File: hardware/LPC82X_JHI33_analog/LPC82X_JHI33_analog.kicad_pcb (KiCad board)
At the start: 2 copper layers, 23.6 x 23.5 mm, 24 parts, among them J1 LPC82XJHI33_LEFT, J2 LPC82XJHI33_RIGHT, J3 JTAG_2X05, U1 LPC824M201JHI33, Y1 12MHz

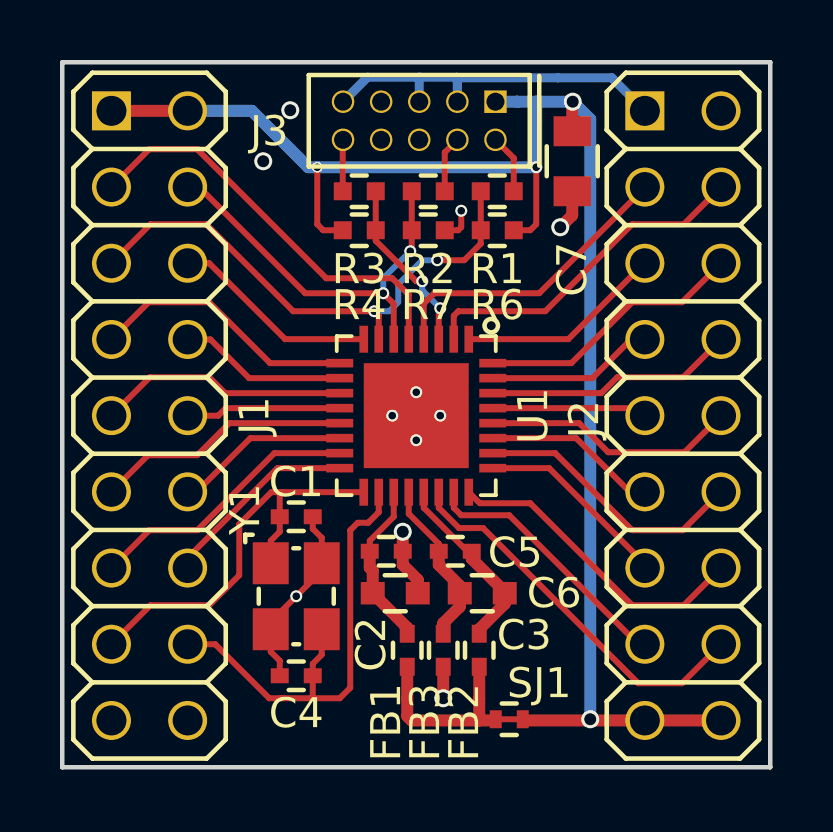
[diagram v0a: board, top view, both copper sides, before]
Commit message: updated schematic, partial layout of new planes and reduction of components
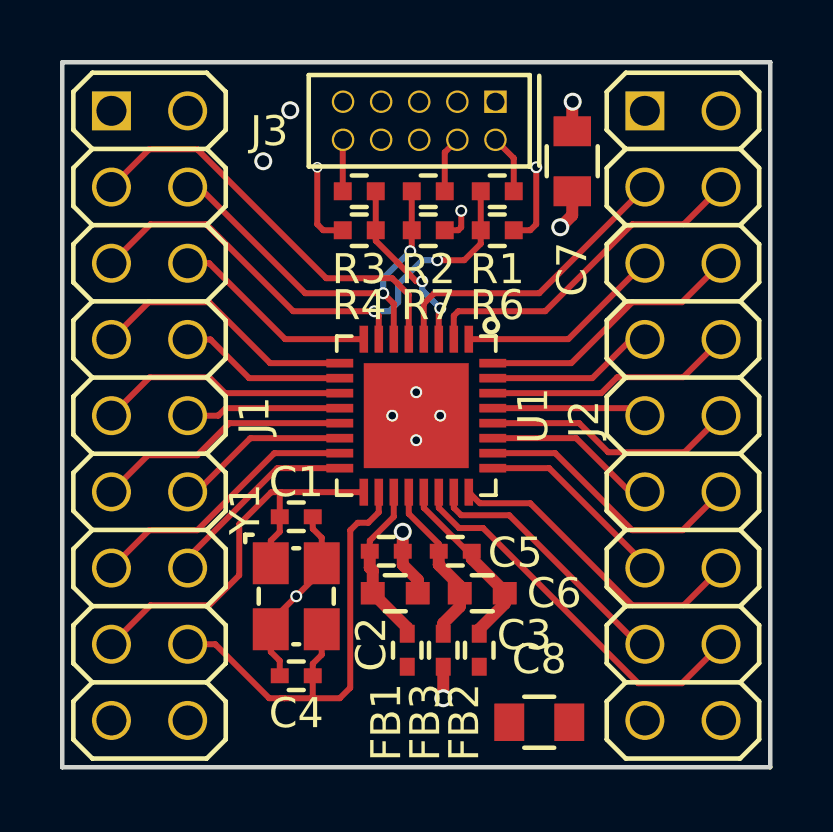
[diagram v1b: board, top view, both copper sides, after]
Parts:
- removed SJ1: SolderJumper_2way_1conn, SquantorSpecial:solder_jumper_2way_conn
- added C8: 10u, SquantorRcl:C_0805, F.Cu at (93.0, 116.9)
- N2: value 20190411 -> 20190412
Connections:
- FB1 pad 2: Net-(FB1-Pad2) -> /VDD
- FB2 pad 2: Net-(FB1-Pad2) -> /AVDD
- FB3 pad 2: /VSS -> /AVSS
- J1 pad 17: /VSS -> /AVSS
- J1 pad 18: /VSS -> /AVSS
- J2 pad 17: /VDD -> /AVDD
- J2 pad 18: /VDD -> /AVDD
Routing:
- net /VDD: track 53.8 -> 6.57 mm, vias 4 -> 3
- net /VSS: track 24.8 -> 11.0 mm, vias 11 -> 10
- net Net-(FB1-Pad2): track 6.46 -> 0.00 mm
- net /AVSS: track 0.00 -> 1.05 mm, vias 0 -> 1
- added copper zone on In1.Cu, net /AVSS
- added copper zone on In1.Cu, net /VSS
- removed copper zone on B.Cu, net /VSS
- removed copper zone on F.Cu, net /VSS
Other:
- copper layers 2 -> 4

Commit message: updated to named pcb connectors, further plane addition, inital silk placement
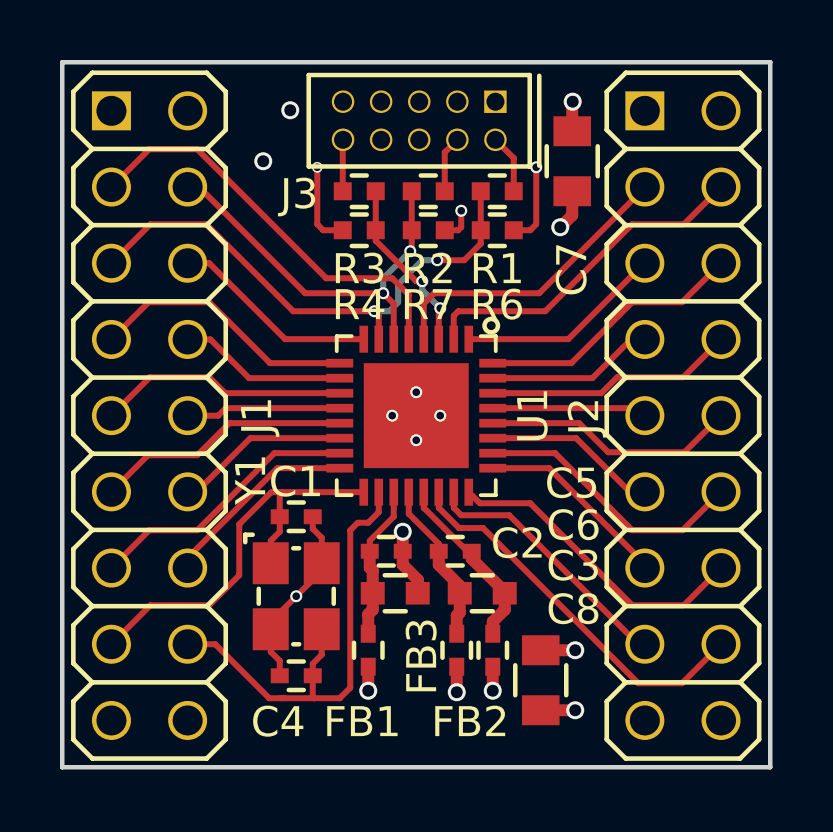
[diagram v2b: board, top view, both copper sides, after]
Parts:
- J1: footprint SquantorConnectorsNamed:LPC82XJHI33_breakout_left -> SquantorConnectorsNamed:LPC82XJHI33_breakout_analog_left
- J2: footprint SquantorConnectorsNamed:LPC82XJHI33_breakout_right -> SquantorConnectorsNamed:LPC82XJHI33_breakout_analog_right
- moved C8 1.40 mm to (93.0, 115.5), turned to 270 degrees
- moved FB1 1.30 mm to (87.3, 114.5)
- moved FB2 0.45 mm to (91.5, 114.5)
- moved FB3 0.45 mm to (90.2, 114.5)
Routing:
- net /AVDD: track 0.00 -> 1.95 mm, vias 0 -> 2
- net /AVSS: track 1.05 -> 2.00 mm, vias 1 -> 2
- net /VDD: track 6.57 -> 7.37 mm, vias 3 -> 4
- added copper zone on In2.Cu, net /AVDD
- added copper zone on In2.Cu, net /VDD
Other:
- rule pad_to_mask_clearance: 0.1 -> 0.05
- rule solder_mask_min_width: 0.1 -> 0.05

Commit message: silk placement completed
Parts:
- moved N1 4.10 mm to (88.7, 102.6)
- moved N2 3.74 mm to (88.7, 113.4), turned to 270 degrees

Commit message: updated versionnumber
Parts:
- N2: value 20190412 -> 20190418
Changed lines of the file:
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@@
       (effects (font (size 1 1) (thickness 0.15)) (justify mirror))
     )
-    (fp_text value 20190412 (at -0.4 0.137362 270) (layer B.SilkS)
+    (fp_text value 20190418 (at -0.4 0.137362 270) (layer B.SilkS)
       (effects (font (size 1 1) (thickness 0.15)) (justify mirror))
     )
